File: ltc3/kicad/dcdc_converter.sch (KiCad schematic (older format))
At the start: 8 parts, among them U3 PTN78020W

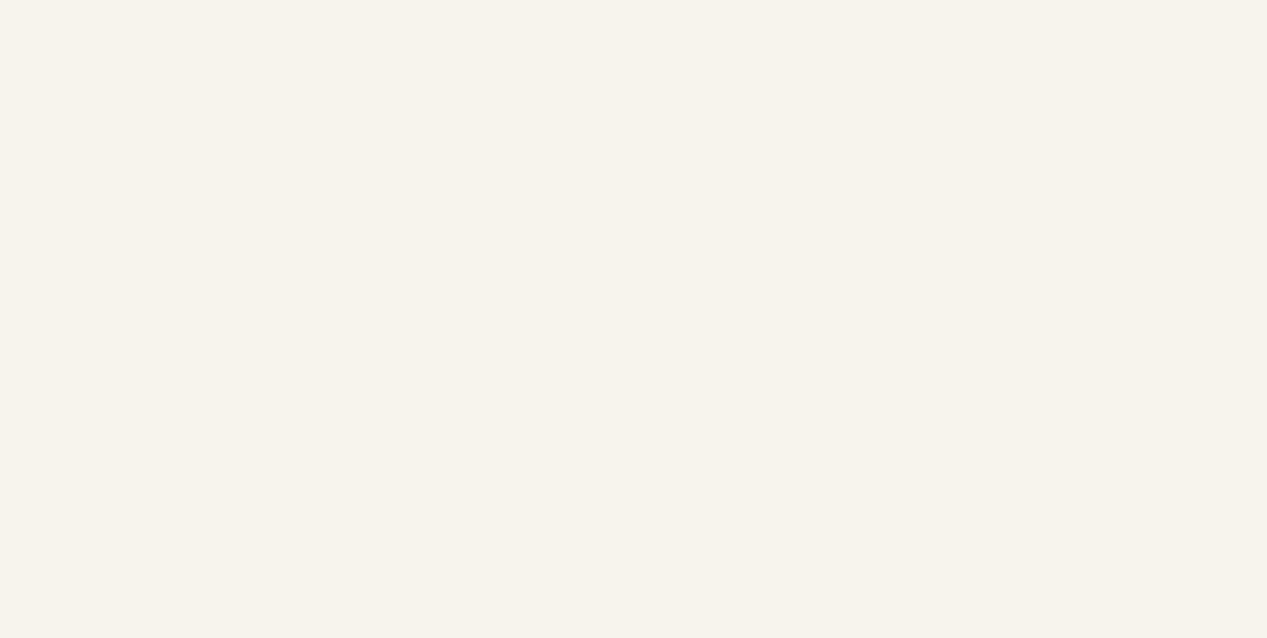
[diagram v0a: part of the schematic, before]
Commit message: LTC3 design progress: added 12V DC-DC converter; prettified top-level schematic. Requirements Spec calls for 12VDC external power.  Batteries are now 28.8VDC (nominal), so we'll need a third converter.
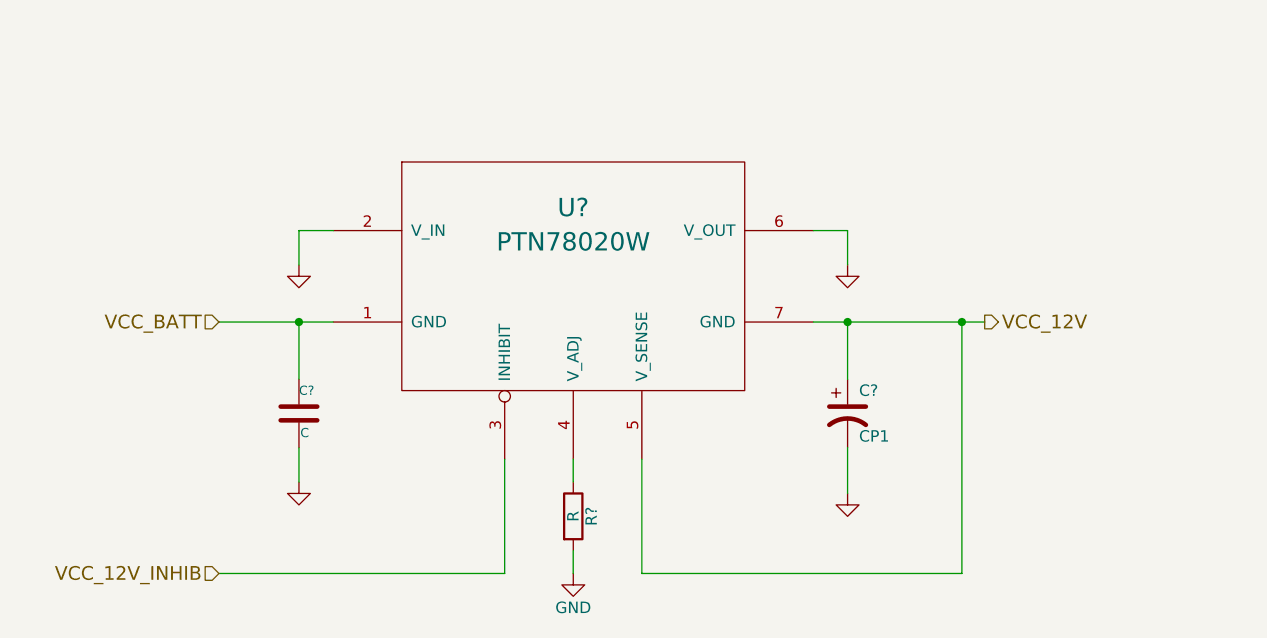
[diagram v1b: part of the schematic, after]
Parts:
- added C?: CP1, ~, symbol CP1
- added C?: C, ~, symbol C
- added R?: R, symbol R
- added U?: PTN78020W, ~, symbol PTN78020W
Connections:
- net GND: now also C?.2, C?.2, R?.2, U?.2 (V_IN), U?.6 (V_OUT)
- net VCC_BATT: now also C?.1, U?.1 (GND)
- new net: R?.1, U?.4 (V_ADJ)
- new net VCC_12V: C?.1, U?.5 (V_SENSE), U?.7 (GND)
- new net VCC_12V_INHIB: U?.3 (INHIBIT)
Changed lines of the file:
@@
 LIBS:contrib
 LIBS:valves
+LIBS:LTC3
 LIBS:Launch_Tower_Computer_III-cache
 EELAYER 25 0
@@
 	1    0    0    -1
 $EndComp
+Text HLabel 6550 7100 2    60   Output ~ 0
+VCC_12V
+Text HLabel 3200 7100 0    60   Input ~ 0
+VCC_BATT
+$Comp
+L PTN78020W U?
+U 1 1 55936D69
+P 4750 6900
+F 0 "U?" H 4750 7200 80  0000 C CNN
+F 1 "PTN78020W" H 4750 7050 80  0000 C CNN
+F 2 "~" H 4750 6950 60  0000 C CNN
+F 3 "~" H 4750 6950 60  0000 C CNN
+	1    4750 6900
+	1    0    0    -1
+$EndComp
+$Comp
+L GND #PWR?
+U 1 1 55936D6F
+P 3550 6850
+F 0 "#PWR?" H 3550 6850 30  0001 C CNN
+F 1 "GND" H 3550 6780 30  0001 C CNN
+F 2 "" H 3550 6850 60  0000 C CNN
+F 3 "" H 3550 6850 60  0000 C CNN
+	1    3550 6850
+	1    0    0    -1
+$EndComp
+$Comp
+L GND #PWR?
+U 1 1 55936D75
+P 5950 6850
+F 0 "#PWR?" H 5950 6850 30  0001 C CNN
+F 1 "GND" H 5950 6780 30  0001 C CNN
+F 2 "" H 5950 6850 60  0000 C CNN
+F 3 "" H 5950 6850 60  0000 C CNN
+	1    5950 6850
+	1    0    0    -1
+$EndComp
+Wire Wire Line
+	3700 6700 3550 6700
+Wire Wire Line
+	3550 6700 3550 6850
+Wire Wire Line
+	5800 6700 5950 6700
+Wire Wire Line
+	5950 6700 5950 6850
+Wire Wire Line
+	5800 7100 6550 7100
+Wire Wire Line
+	3200 7100 3700 7100
+$Comp
+L CP1 C?
+U 1 1 55936D81
+P 5950 7500
+F 0 "C?" H 6000 7600 50  0000 L CNN
+F 1 "CP1" H 6000 7400 50  0000 L CNN
+F 2 "~" H 5950 7500 60  0000 C CNN
+F 3 "~" H 5950 7500 60  0000 C CNN
+	1    5950 7500
+	1    0    0    -1
+$EndComp
+$Comp
+L GND #PWR?
+U 1 1 55936D87
+P 5950 7850
+F 0 "#PWR?" H 5950 7850 30  0001 C CNN
+F 1 "GND" H 5950 7780 30  0001 C CNN
+F 2 "" H 5950 7850 60  0000 C CNN
+F 3 "" H 5950 7850 60  0000 C CNN
+	1    5950 7850
+	1    0    0    -1
+$EndComp
+Wire Wire Line
+	5950 7350 5950 7100
+Connection ~ 5950 7100
+Wire Wire Line
+	5950 7650 5950 7850
+$Comp
+L C C?
+U 1 1 55936D90
+P 3550 7500
+F 0 "C?" H 3550 7600 40  0000 L CNN
+F 1 "C" H 3556 7415 40  0000 L CNN
+F 2 "~" H 3588 7350 30  0000 C CNN
+F 3 "~" H 3550 7500 60  0000 C CNN
+	1    3550 7500
+	1    0    0    -1
+$EndComp
+$Comp
+L GND #PWR?
+U 1 1 55936D96
+P 3550 7800
+F 0 "#PWR?" H 3550 7800 30  0001 C CNN
+F 1 "GND" H 3550 7730 30  0001 C CNN
+F 2 "" H 3550 7800 60  0000 C CNN
+F 3 "" H 3550 7800 60  0000 C CNN
+	1    3550 7800
+	1    0    0    -1
+$EndComp
+Wire Wire Line
+	3550 7800 3550 7650
+Wire Wire Line
+	3550 7350 3550 7100
+Connection ~ 3550 7100
+$Comp
+L R R?
+U 1 1 55936D9F
+P 4750 7950
+F 0 "R?" V 4830 7950 50  0000 C CNN
+F 1 "R" V 4750 7950 50  0000 C CNN
+F 2 "" V 4680 7950 30  0000 C CNN
+F 3 "" H 4750 7950 30  0000 C CNN
+	1    4750 7950
+	1    0    0    -1
+$EndComp
+$Comp
+L GND #PWR?
+U 1 1 55936DA5
+P 4750 8200
+F 0 "#PWR?" H 4750 7950 50  0001 C CNN
+F 1 "GND" H 4750 8050 50  0000 C CNN
+F 2 "" H 4750 8200 60  0000 C CNN
+F 3 "" H 4750 8200 60  0000 C CNN
+	1    4750 8200
+	1    0    0    -1
+$EndComp
+Wire Wire Line
+	4750 8200 4750 8100
+Wire Wire Line
+	4750 7800 4750 7700
+Text HLabel 3200 8200 0    60   Input ~ 0
+VCC_12V_INHIB
+Wire Wire Line
+	4450 7700 4450 8200
+Wire Wire Line
+	4450 8200 3200 8200
+Wire Wire Line
+	5050 7700 5050 8200
+Wire Wire Line
+	5050 8200 6450 8200
+Wire Wire Line
+	6450 8200 6450 7100
+Connection ~ 6450 7100
 $EndSCHEMATC

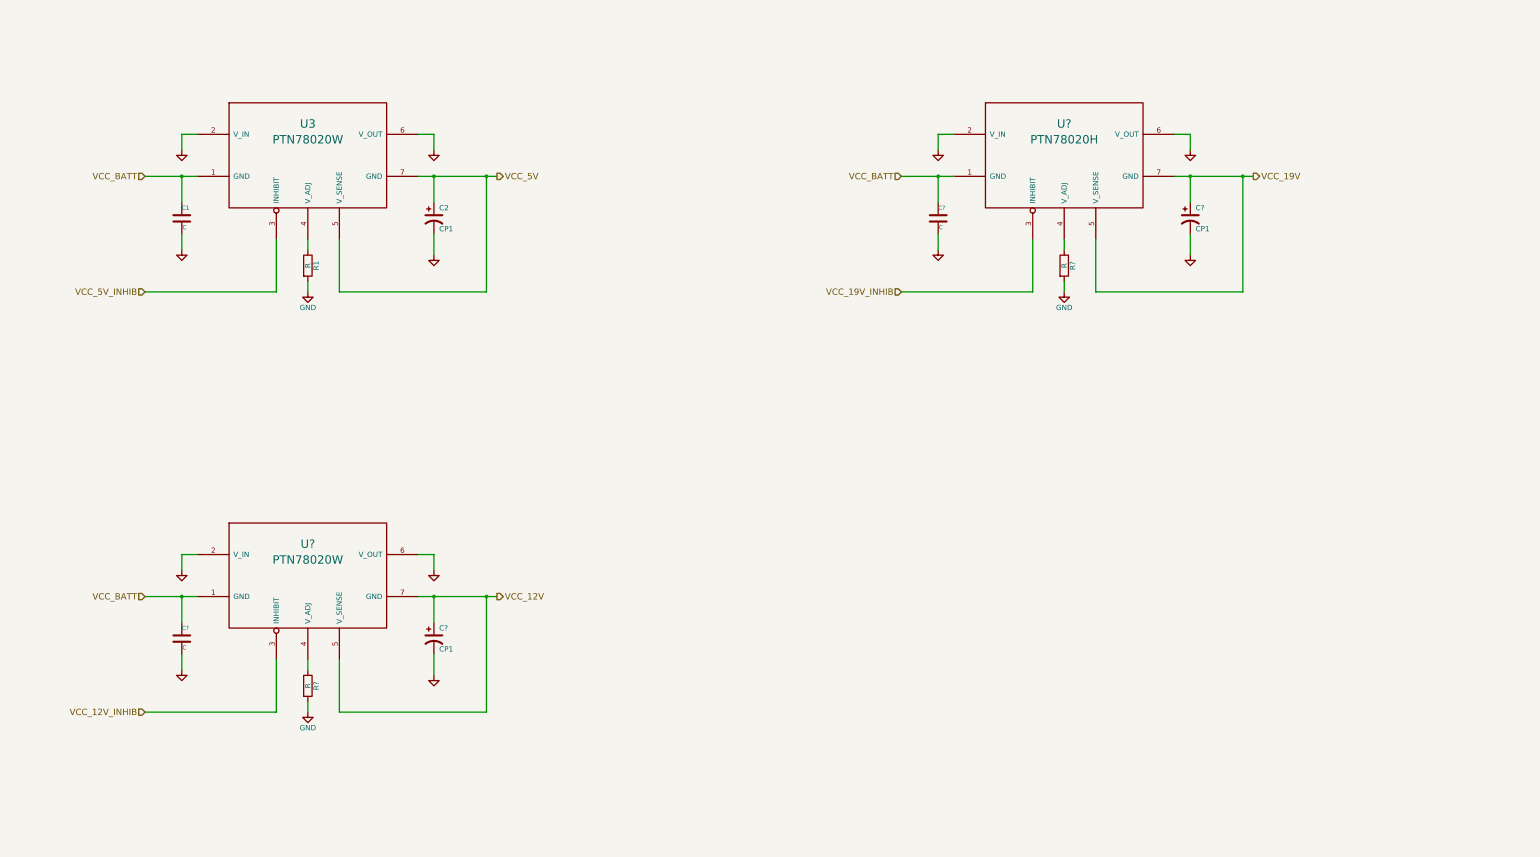
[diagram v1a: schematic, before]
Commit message: More LTC3 design: completed DC-DC converter schematics. Mostly.  A thorough review of the PTN78020[WH] datasheet followed by a once-over of the schematic wouldn't hurt.
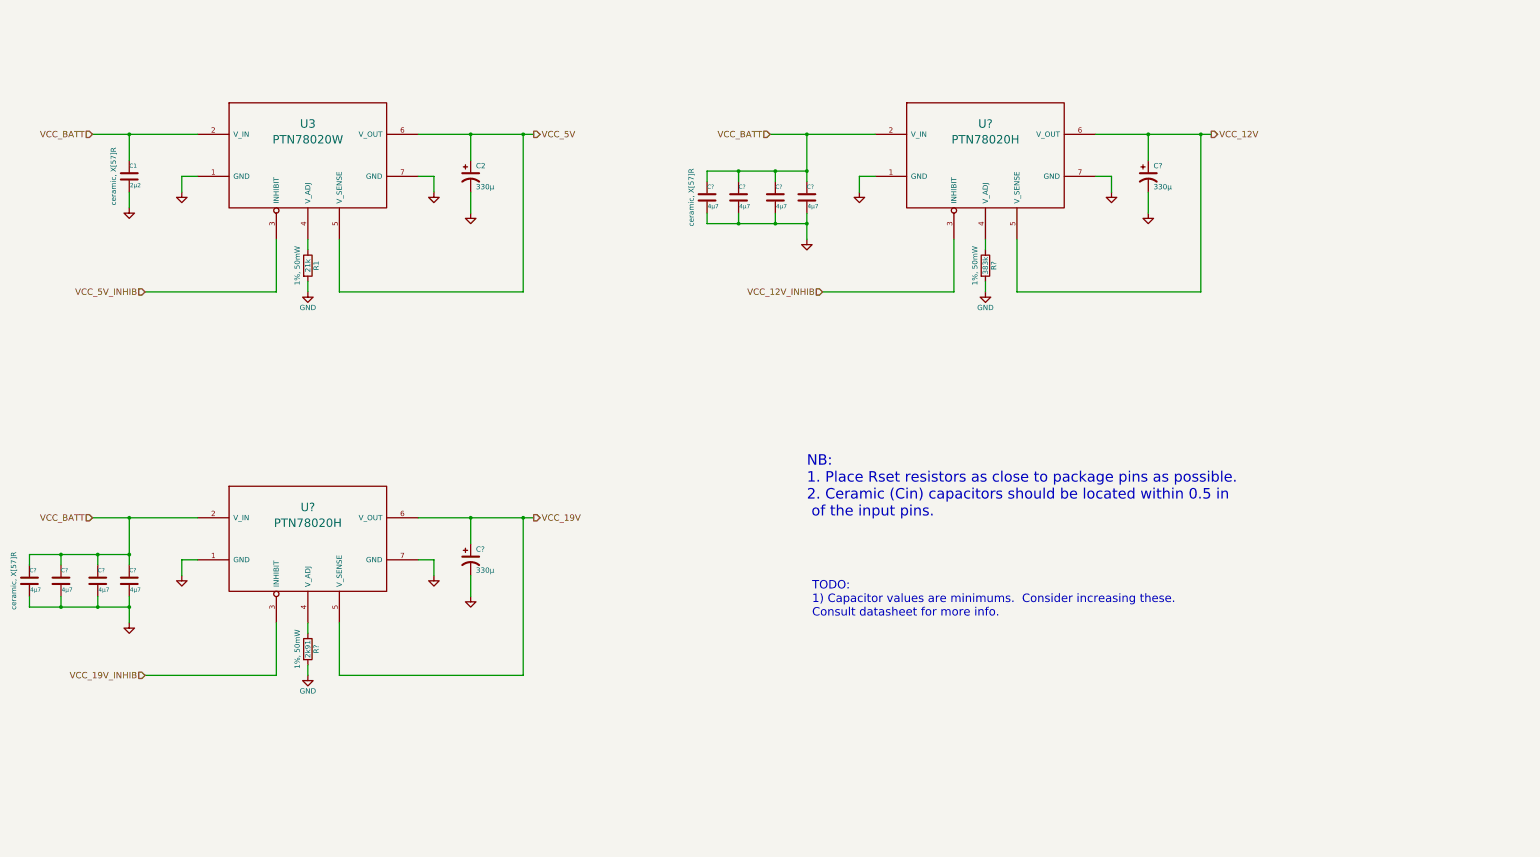
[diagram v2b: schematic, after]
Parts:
- removed C? (x2): CP1, ~, symbol CP1
- removed C? (x2): C, ~, symbol C
- removed R? (x2): R, symbol R
- removed U?: PTN78020H, symbol PTN78020H
- removed U?: PTN78020W, ~, symbol PTN78020W
- added C? (x2): 330μ, ~, symbol CP1
- added C? (x8): 4μ7, ~, symbol C
- added R?: 383k, symbol R
- added R?: 2k91, symbol R
- added U? (x2): PTN78020H, ~, symbol PTN78020H
- C1: value C -> 2μ2; Note (none) -> ceramic, X[57]R
- C2: value CP1 -> 330μ
- R1: value R -> 21k; Note (none) -> 1%, 50mW
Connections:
- net GND: now also U3.1 (GND), U3.7 (GND), C?.2, C?.2, C?.2, C?.2, C?.2, C?.2, C?.2, C?.2, C?.2, C?.2, R?.2, R?.2, U?.1 (GND), U?.1 (GND), U?.7 (GND), U?.7 (GND); no longer U3.2 (V_IN), U3.6 (V_OUT)
- net VCC_12V: now also C?.1, U?.5 (V_SENSE), U?.6 (V_OUT)
- net VCC_12V_INHIB: now also U?.3 (INHIBIT)
- net VCC_19V: now also C?.1, U?.5 (V_SENSE), U?.6 (V_OUT)
- net VCC_19V_INHIB: now also U?.3 (INHIBIT)
- net VCC_5V: now also U3.6 (V_OUT); no longer U3.7 (GND)
- net VCC_BATT: now also U3.2 (V_IN), C?.1, C?.1, C?.1, C?.1, C?.1, C?.1, C?.1, C?.1, U?.2 (V_IN), U?.2 (V_IN); no longer U3.1 (GND)
- new net: R?.1, U?.4 (V_ADJ) (x2)
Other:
- note added: "NB:\n1. Place Rset resistors as close to package pins as possible.\n2. Ceramic (Cin) capacitors should be located within 0.5 in\n of the input pins."
- note added: "TODO:\n1) Capacitor values are minimums. Consider increasing these.\nConsult datasheet for more info."
- moved on the sheet: C1, C2

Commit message: Minor adjustments to LTC3 DC-DC converter schematics. Fixed the V_out sense lines; added a few helpful notes.
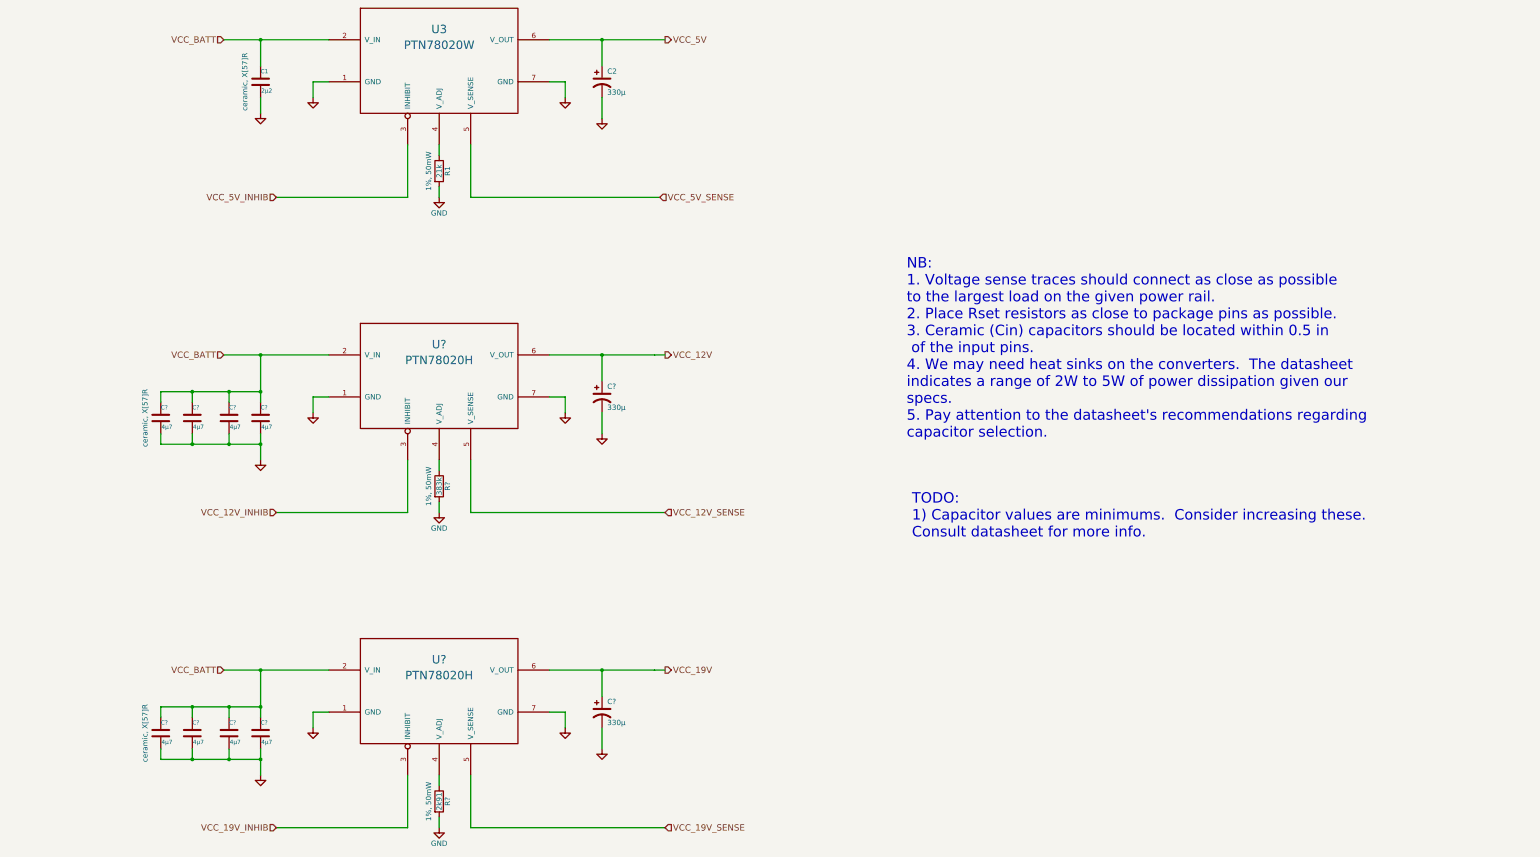
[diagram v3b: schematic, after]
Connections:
- net VCC_12V: no longer U?.5 (V_SENSE)
- net VCC_19V: no longer U?.5 (V_SENSE)
- net VCC_5V: no longer U3.5 (V_SENSE)
- new net VCC_12V_SENSE: U?.5 (V_SENSE)
- new net VCC_19V_SENSE: U?.5 (V_SENSE)
- new net VCC_5V_SENSE: U3.5 (V_SENSE)
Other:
- note added: "NB:\n1. Voltage sense traces should connect as close as possible\nto the largest load on the given power rail.\n2. Place Rset resistors as close to package pins as possible.\n3. Ceramic (Cin) capacitors should be located within 0.5 in\n of the input pins.\n4. We may need heat sinks on the converters. The datasheet\nindicates a range of 2W to 5W of power dissipation given our\nspecs.\n5. Pay atten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"
- note removed: "NB:\n1. Place Rset resistors as close to package pins as possible.\n2. Ceramic (Cin) capacitors should be located within 0.5 in\n of the input pins."
- moved on the sheet: C1, C2, C?, R1, R?, U3, U?
